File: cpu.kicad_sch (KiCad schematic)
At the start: 19 parts, among them J1 USB_C_Receptacle, SW1 TL3342F160QG/TR, U4 RP2040, U5 LM4040DBZ-3, U6 W25Q32JVSS, Y1 Crystal

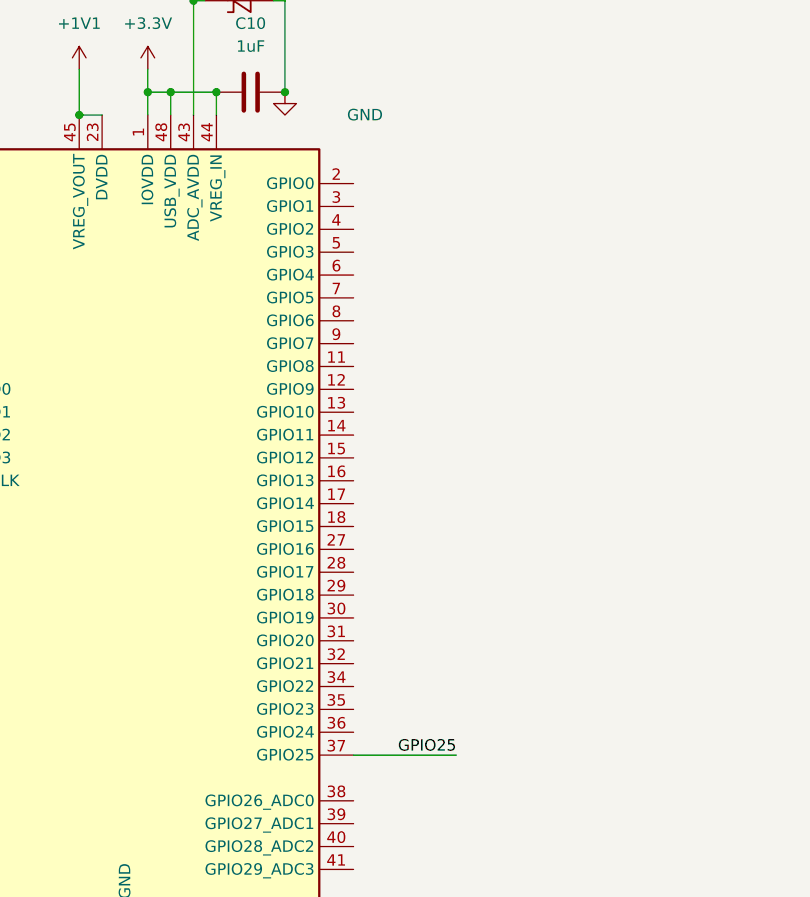
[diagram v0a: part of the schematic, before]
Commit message: Expanded IO
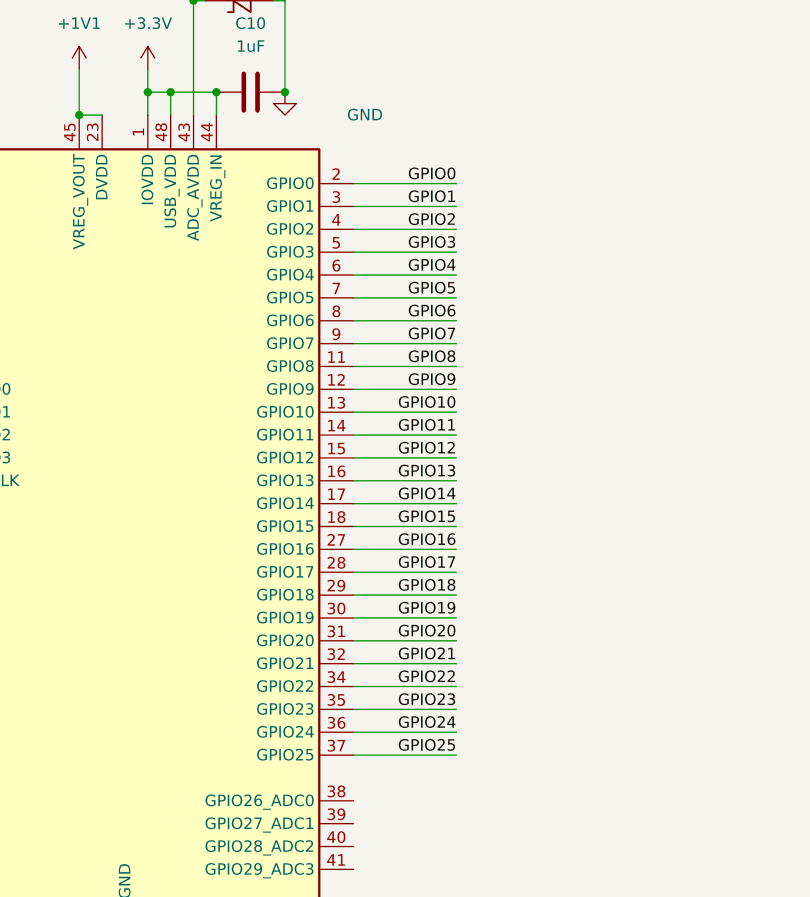
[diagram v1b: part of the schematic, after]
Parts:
- SW1: footprint SW_TL3342F160QG/TR -> TL3342F160QG_TR:SW_TL3342F160QG%2fTR
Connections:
- net GPIO8: now reaches U4.11 (GPIO8)
- net GPIO9: now reaches U4.12 (GPIO9)
- net GPIO10: now reaches U4.13 (GPIO10)
- net GPIO11: now reaches U4.14 (GPIO11)
- net GPIO12: now reaches U4.15 (GPIO12)
- net GPIO13: now reaches U4.16 (GPIO13)
- net GPIO14: now reaches U4.17 (GPIO14)
- net GPIO15: now reaches U4.18 (GPIO15)
- net GPIO0: now reaches U4.2 (GPIO0)
- net GPIO16: now reaches U4.27 (GPIO16)
- net GPIO17: now reaches U4.28 (GPIO17)
- net GPIO18: now reaches U4.29 (GPIO18)
- net GPIO1: now reaches U4.3 (GPIO1)
- net GPIO19: now reaches U4.30 (GPIO19)
- net GPIO20: now reaches U4.31 (GPIO20)
- net GPIO21: now reaches U4.32 (GPIO21)
- net GPIO22: now reaches U4.34 (GPIO22)
- net GPIO23: now reaches U4.35 (GPIO23)
- net GPIO24: now reaches U4.36 (GPIO24)
- net GPIO2: now reaches U4.4 (GPIO2)
- net GPIO3: now reaches U4.5 (GPIO3)
- net GPIO4: now reaches U4.6 (GPIO4)
- net GPIO5: now reaches U4.7 (GPIO5)
- net GPIO6: now reaches U4.8 (GPIO6)
- net GPIO7: now reaches U4.9 (GPIO7)

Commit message: Rev 1.0
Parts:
- added C17, C18, C19, C20, C21, C22, C23, C24: 0.1uF, Capacitor_SMD:C_0201_0603Metric, symbol Device:C
- added R15: 10k, Resistor_SMD:R_0603_1608Metric, symbol Device:R
- added SW2: TL3342F160QG/TR, TL3342F160QG_TR:SW_TL3342F160QG%2fTR, symbol TL3342F160QG_TR:TL3342F160QG/TR
- C10, C14: footprint (none) -> Capacitor_SMD:C_0201_0603Metric
- C11, C13: value 2u2F -> 27pF; footprint (none) -> Capacitor_SMD:C_0201_0603Metric
- C12: value 2u2F -> 0.1uF; footprint (none) -> Capacitor_SMD:C_0201_0603Metric
- D5: footprint (none) -> LED_SMD:LED_0201_0603Metric
- J1: footprint (none) -> Connector_USB:USB_C_Receptacle_HRO_TYPE-C-31-M-12
- R3, R4, R5, R6, R7, R8, R9: footprint (none) -> Resistor_SMD:R_0603_1608Metric
- Y1: footprint (none) -> Crystal:Crystal_SMD_3225-4Pin_3.2x2.5mm
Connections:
- net +1V1: now also C23.1, C24.1
- net +3.3V: now also C17.1, C18.1, C19.1, C20.1, C21.1, C22.1, R15.1
- net GND: now also C17.2, C18.2, C19.2, C20.2, C21.2, C22.2, C23.2, C24.2, SW2.1, SW2.2
- net RUN: now reaches U4.26 (RUN)
- net RUN: now also R15.2, SW2.3, SW2.4
- net GPIO26: now reaches U4.38 (GPIO26_ADC0)
- net GPIO27: now reaches U4.39 (GPIO27_ADC1)
- net GPIO28: now reaches U4.40 (GPIO28_ADC2)
- net GPIO29: now reaches U4.41 (GPIO29_ADC3)
- no-connect marks 0 -> 2
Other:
- note added: "Close to ADC_AVDD"
- note added: "Close to DVDD"
- note added: "Close to all IOVDD"
- title: (none) -> Iron Warriors v2.0 
- moved on the sheet: C10, C11, C13, C14, D5, R3, R4, R5, R8, R9, SW1, U4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

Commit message: Initial PCB view
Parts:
- C10, C11, C12, C13, C14, C17, C18, C19, C20, C21, C22, C23, C24: footprint Capacitor_SMD:C_0201_0603Metric -> Capacitor_SMD:C_0603_1608Metric
- D5: footprint LED_SMD:LED_0201_0603Metric -> LED_SMD:LED_0603_1608Metric
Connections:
- net XIN: now also Y1.2; no longer Y1.1
- net XOUT: now also Y1.1; no longer Y1.2
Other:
- moved on the sheet: Y1
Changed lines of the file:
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@@
   (title_block
     (title "Iron Warriors v2.0 ")
-    (date "2022-12-08")
+    (date "2022-12-13")
     (rev "1.0")
   )
@@
     (effects (font (size 1.27 1.27)) (justify left bottom))
   )
+  (hierarchical_label "GPIO23" (shape output) (at 141.605 114.3 0)
+    (effects (font (size 1.27 1.27)) (justify left))
+  )
+  (hierarchical_label "GPIO20" (shape output) (at 141.605 106.68 0)
+    (effects (font (size 1.27 1.27)) (justify left))
+  )
+  (hierarchical_label "GPIO21" (shape input) (at 141.605 109.22 0)
+    (effects (font (size 1.27 1.27)) (justify left))
+  )
+  (hierarchical_label "GPIO22" (shape input) (at 141.605 111.76 0)
+    (effects (font (size 1.27 1.27)) (justify left))
+  )
+  (hierarchical_label "GPIO25" (shape input) (at 141.605 119.38 0)
+    (effects (font (size 1.27 1.27)) (justify left))
+  )
+  (hierarchical_label "GPIO24" (shape input) (at 141.605 116.84 0)
+    (effects (font (size 1.27 1.27)) (justify left))
+  )
   (symbol (lib_id "Device:R") (at 218.44 25.4 0) (unit 1)
     (in_bom yes) (on_board yes)
@@
     (property "Reference" "C10" (id 0) (at 118.745 38.1 90))
     (property "Value" "1uF" (id 1) (at 118.745 40.64 90))
-    (property "Footprint" "Capacitor_SMD:C_0201_0603Metric" (id 2) (at 114.935 46.6852 0)
+    (property "Footprint" "Capacitor_SMD:C_0603_1608Metric" (id 2) (at 114.935 46.6852 0)
       (effects (font (size 1.27 1.27)) hide)
     )
@@
       (effects (font (size 1.27 1.27)) (justify left))
     )
-    (property "Footprint" "Capacitor_SMD:C_0201_0603Metric" (id 2) (at 84.7852 170.18 0)
+    (property "Footprint" "Capacitor_SMD:C_0603_1608Metric" (id 2) (at 84.7852 170.18 0)
       (effects (font (size 1.27 1.27)) hide)
     )
@@
     (property "Reference" "D5" (id 0) (at 242.2525 59.055 0))
     (property "Value" "LED" (id 1) (at 242.2525 61.595 0))
-    (property "Footprint" "LED_SMD:LED_0201_0603Metric" (id 2) (at 240.665 66.675 0)
+    (property "Footprint" "LED_SMD:LED_0603_1608Metric" (id 2) (at 240.665 66.675 0)
       (effects (font (size 1.27 1.27)) hide)
     )
@@
       (effects (font (size 1.27 1.27)) (justify left))
     )
-    (property "Footprint" "Capacitor_SMD:C_0201_0603Metric" (id 2) (at 115.2652 170.18 0)
+    (property "Footprint" "Capacitor_SMD:C_0603_1608Metric" (id 2) (at 115.2652 170.18 0)
       (effects (font (size 1.27 1.27)) hide)
     )
@@
       (effects (font (size 1.27 1.27)) (justify left))
     )
-    (property "Footprint" "Capacitor_SMD:C_0201_0603Metric" (id 2) (at 46.6852 170.18 0)
+    (property "Footprint" "Capacitor_SMD:C_0603_1608Metric" (id 2) (at 46.6852 170.18 0)
       (effects (font (size 1.27 1.27)) hide)
     )
@@
       (effects (font (size 1.27 1.27)) (justify left))
     )
-    (property "Footprint" "Capacitor_SMD:C_0201_0603Metric" (id 2) (at 247.9802 106.045 0)
+    (property "Footprint" "Capacitor_SMD:C_0603_1608Metric" (id 2) (at 247.9802 106.045 0)
       (effects (font (size 1.27 1.27)) hide)
     )
@@
     (pin "1")
   )
-  (symbol (lib_id "Device:Crystal") (at 238.125 98.425 0) (unit 1)
-    (in_bom yes) (on_board yes) (fields_autoplaced)
-    (property "Reference" "Y1" (id 0) (at 238.125 90.805 0))
-    (property "Value" "Crystal" (id 1) (at 238.125 93.345 0))
+  (symbol (lib_id "Device:Crystal") (at 238.125 98.425 180) (unit 1)
+    (in_bom yes) (on_board yes) (fields_autoplaced)
+    (property "Reference" "Y1" (id 0) (at 238.125 90.17 0))
+    (property "Value" "Crystal" (id 1) (at 238.125 92.71 0))
     (property "Footprint" "Crystal:Crystal_SMD_3225-4Pin_3.2x2.5mm" (id 2) (at 238.125 98.425 0)
       (effects (font (size 1.27 1.27)) hide)
@@
       (effects (font (size 1.27 1.27)) (justify left))
     )
-    (property "Footprint" "Capacitor_SMD:C_0201_0603Metric" (id 2) (at 97.4852 170.18 0)
+    (property "Footprint" "Capacitor_SMD:C_0603_1608Metric" (id 2) (at 97.4852 170.18 0)
       (effects (font (size 1.27 1.27)) hide)
     )
@@
       (effects (font (size 1.27 1.27)) (justify left))
     )
-    (property "Footprint" "Capacitor_SMD:C_0201_0603Metric" (id 2) (at 59.3852 170.18 0)
+    (property "Footprint" "Capacitor_SMD:C_0603_1608Metric" (id 2) (at 59.3852 170.18 0)
       (effects (font (size 1.27 1.27)) hide)
     )
@@
       (effects (font (size 1.27 1.27)) (justify left))
     )
-    (property "Footprint" "Capacitor_SMD:C_0201_0603Metric" (id 2) (at 253.0602 26.67 0)
+    (property "Footprint" "Capacitor_SMD:C_0603_1608Metric" (id 2) (at 253.0602 26.67 0)
       (effects (font (size 1.27 1.27)) hide)
     )
@@
       (effects (font (size 1.27 1.27)) (justify left))
     )
-    (property "Footprint" "Capacitor_SMD:C_0201_0603Metric" (id 2) (at 228.9302 106.045 0)
+    (property "Footprint" "Capacitor_SMD:C_0603_1608Metric" (id 2) (at 228.9302 106.045 0)
       (effects (font (size 1.27 1.27)) hide)
     )
@@
       (effects (font (size 1.27 1.27)) (justify left))
     )
-    (property "Footprint" "Capacitor_SMD:C_0201_0603Metric" (id 2) (at 33.9852 170.18 0)
+    (property "Footprint" "Capacitor_SMD:C_0603_1608Metric" (id 2) (at 33.9852 170.18 0)
       (effects (font (size 1.27 1.27)) hide)
     )
@@
       (effects (font (size 1.27 1.27)) (justify left))
     )
-    (property "Footprint" "Capacitor_SMD:C_0201_0603Metric" (id 2) (at 72.0852 170.18 0)
+    (property "Footprint" "Capacitor_SMD:C_0603_1608Metric" (id 2) (at 72.0852 170.18 0)
       (effects (font (size 1.27 1.27)) hide)
     )
@@
       (effects (font (size 1.27 1.27)) (justify left))
     )
-    (property "Footprint" "Capacitor_SMD:C_0201_0603Metric" (id 2) (at 141.9352 170.18 0)
+    (property "Footprint" "Capacitor_SMD:C_0603_1608Metric" (id 2) (at 141.9352 170.18 0)
       (effects (font (size 1.27 1.27)) hide)
     )
@@
       (effects (font (size 1.27 1.27)) (justify left))
     )
-    (property "Footprint" "Capacitor_SMD:C_0201_0603Metric" (id 2) (at 154.6352 170.18 0)
-      (effects (font (size 1.27 1.27)) hide)
-    )
+    (property "Footprint" "Capacitor_SMD:C_0603_1608Metric" (id 2) (at 154.6352 170.18 0)
+      (effects (font (size 1.27 1.27)) hide)
+    )

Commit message: First full version of the PCB
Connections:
- net GPIO11: now also R8.2
- net GPIO25: no longer R8.2
- net D+: now reaches R3.2, U4.47 (USB_DP)
- net D-: now reaches R4.2, U4.46 (USB_DM)
- no-connect marks 2 -> 14
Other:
- moved on the sheet: R3, R4
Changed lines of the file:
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@@
   (junction (at 45.72 162.56) (diameter 0) (color 0 0 0 0)
   )
+  (junction (at 109.855 45.72) (diameter 0) (color 0 0 0 0)
+  )
+  (junction (at 46.99 39.37) (diameter 0) (color 0 0 0 0)
+  )
+  (junction (at 162.56 21.59) (diameter 0) (color 0 0 0 0)
+  )
+  (junction (at 114.935 45.72) (diameter 0) (color 0 0 0 0)
+  )
+  (junction (at 170.18 44.45) (diameter 0) (color 0 0 0 0)
+  )
+  (junction (at 122.555 45.72) (diameter 0) (color 0 0 0 0)
+  )
+  (junction (at 31.75 87.63) (diameter 0) (color 0 0 0 0)
+  )
+  (junction (at 107.315 45.72) (diameter 0) (color 0 0 0 0)
+  )
+  (junction (at 162.56 53.975) (diameter 0) (color 0 0 0 0)
+  )
+  (junction (at 58.42 162.56) (diameter 0) (color 0 0 0 0)
+  )
   (junction (at 46.99 36.83) (diameter 0) (color 0 0 0 0)
   )
-  (junction (at 31.75 87.63) (diameter 0) (color 0 0 0 0)
-  )
-  (junction (at 109.855 45.72) (diameter 0) (color 0 0 0 0)
-  )
-  (junction (at 162.56 21.59) (diameter 0) (color 0 0 0 0)
-  )
-  (junction (at 114.935 45.72) (diameter 0) (color 0 0 0 0)
-  )
-  (junction (at 170.18 44.45) (diameter 0) (color 0 0 0 0)
-  )
-  (junction (at 46.99 39.37) (diameter 0) (color 0 0 0 0)
-  )
-  (junction (at 122.555 45.72) (diameter 0) (color 0 0 0 0)
-  )
-  (junction (at 107.315 45.72) (diameter 0) (color 0 0 0 0)
-  )
-  (junction (at 162.56 53.975) (diameter 0) (color 0 0 0 0)
-  )
-  (junction (at 58.42 162.56) (diameter 0) (color 0 0 0 0)
-  )
   (junction (at 79.375 55.88) (diameter 0) (color 0 0 0 0)
   )
@@
   (junction (at 140.97 162.56) (diameter 0) (color 0 0 0 0)
   )
+  (no_connect (at 46.99 46.99))
+  (no_connect (at 46.99 72.39))
+  (no_connect (at 46.99 62.23))
+  (no_connect (at 46.99 29.21))
+  (no_connect (at 46.99 64.77))
+  (no_connect (at 46.99 69.85))
+  (no_connect (at 46.99 77.47))
   (no_connect (at 79.375 121.92))
+  (no_connect (at 46.99 80.01))
+  (no_connect (at 46.99 57.15))
   (no_connect (at 79.375 124.46))
+  (no_connect (at 46.99 54.61))
+  (no_connect (at 46.99 49.53))
+  (no_connect (at 46.99 26.67))
   (wire (pts (xy 109.855 45.72) (xy 107.315 45.72))
     (stroke (width 0) (type default) (color 0 0 0 0))
   )
-  (wire (pts (xy 62.865 63.5) (xy 71.755 63.5))
+  (wire (pts (xy 52.07 63.5) (xy 60.96 63.5))
     (stroke (width 0) (type default) (color 0 0 0 0))
   )
@@
     (stroke (width 0) (type default) (color 0 0 0 0))
   )
+  (wire (pts (xy 68.58 66.04) (xy 79.375 66.04))
+    (stroke (width 0) (type default) (color 0 0 0 0))
+  )
   (wire (pts (xy 79.375 139.7) (xy 104.775 139.7))
     (stroke (width 0) (type default) (color 0 0 0 0))
@@
     (stroke (width 0) (type default) (color 0 0 0 0))
   )
+  (wire (pts (xy 68.58 63.5) (xy 79.375 63.5))
+    (stroke (width 0) (type default) (color 0 0 0 0))
+  )
   (wire (pts (xy 141.605 58.42) (xy 130.175 58.42))
     (stroke (width 0) (type default) (color 0 0 0 0))
   )
-  (wire (pts (xy 62.865 66.04) (xy 71.755 66.04))
+  (wire (pts (xy 52.07 66.04) (xy 60.96 66.04))
     (stroke (width 0) (type default) (color 0 0 0 0))
   )
@@
     (effects (font (size 1.27 1.27)) (justify right bottom))
   )
+  (label "D+" (at 71.755 63.5 0)
+    (effects (font (size 1.27 1.27)) (justify left bottom))
+  )
+  (label "D-" (at 71.755 66.04 0)
+    (effects (font (size 1.27 1.27)) (justify left bottom))
+  )
   (label "QSPI_SD3" (at 264.16 45.72 180)
     (effects (font (size 1.27 1.27)) (justify right bottom))
@@
     (effects (font (size 1.27 1.27)) (justify right bottom))
   )
-  (label "USB_DP" (at 62.865 63.5 0)
+  (label "USB_DP" (at 52.07 63.5 0)
     (effects (font (size 1.27 1.27)) (justify left bottom))
   )
@@
     (effects (font (size 1.27 1.27)) (justify right bottom))
   )
-  (label "USB_DM" (at 62.865 66.04 0)
+  (label "USB_DM" (at 52.07 66.04 0)
     (effects (font (size 1.27 1.27)) (justify left bottom))
   )
@@
     (effects (font (size 1.27 1.27)) (justify right bottom))
   )
-  (label "GPIO25" (at 217.805 66.675 0)
+  (label "GPIO11" (at 217.805 66.675 0)
     (effects (font (size 1.27 1.27)) (justify left bottom))
   )
@@
     (pin "2")
   )
-  (symbol (lib_id "Device:R") (at 75.565 63.5 90) (unit 1)
+  (symbol (lib_id "Device:R") (at 64.77 63.5 90) (unit 1)
     (in_bom yes) (on_board yes)
-    (property "Reference" "R3" (id 0) (at 75.565 60.96 90))
-    (property "Value" "27" (id 1) (at 75.565 63.5 90))
-    (property "Footprint" "Resistor_SMD:R_0603_1608Metric" (id 2) (at 75.565 65.278 90)
-      (effects (font (size 1.27 1.27)) hide)
-    )
-    (property "Datasheet" "~" (id 3) (at 75.565 63.5 0)
+    (property "Reference" "R3" (id 0) (at 64.77 60.96 90))
+    (property "Value" "27" (id 1) (at 64.77 63.5 90))
+    (property "Footprint" "Resistor_SMD:R_0603_1608Metric" (id 2) (at 64.77 65.278 90)
+      (effects (font (size 1.27 1.27)) hide)
+    )
+    (property "Datasheet" "~" (id 3) (at 64.77 63.5 0)
       (effects (font (size 1.27 1.27)) hide)
     )
@@
     )
     (pin "1")
+  )
+  (symbol (lib_id "Device:C") (at 114.3 166.37 0) (unit 1)
+    (in_bom yes) (on_board yes) (fields_autoplaced)
+    (property "Reference" "C22" (id 0) (at 118.11 165.0999 0)
+      (effects (font (size 1.27 1.27)) (justify left))
+    )
+    (property "Value" "0.1uF" (id 1) (at 118.11 167.6399 0)
+      (effects (font (size 1.27 1.27)) (justify left))
+    )
+    (property "Footprint" "Capacitor_SMD:C_0603_1608Metric" (id 2) (at 115.2652 170.18 0)
+      (effects (font (size 1.27 1.27)) hide)
+    )
+    (property "Datasheet" "~" (id 3) (at 114.3 166.37 0)
+      (effects (font (size 1.27 1.27)) hide)
+    )
+    (pin "1")
+    (pin "2")
   )
   (symbol (lib_id "Connector:USB_C_Receptacle") (at 31.75 46.99 0) (unit 1)
@@
     (pin "S1")
   )
-  (symbol (lib_id "Device:C") (at 114.3 166.37 0) (unit 1)
-    (in_bom yes) (on_board yes) (fields_autoplaced)
-    (property "Reference" "C22" (id 0) (at 118.11 165.0999 0)
-      (effects (font (size 1.27 1.27)) (justify left))
-    )
-    (property "Value" "0.1uF" (id 1) (at 118.11 167.6399 0)
-      (effects (font (size 1.27 1.27)) (justify left))
-    )
-    (property "Footprint" "Capacitor_SMD:C_0603_1608Metric" (id 2) (at 115.2652 170.18 0)
-      (effects (font (size 1.27 1.27)) hide)
-    )
-    (property "Datasheet" "~" (id 3) (at 114.3 166.37 0)
-      (effects (font (size 1.27 1.27)) hide)
-    )
-    (pin "1")
-    (pin "2")
-  )
   (symbol (lib_id "power:+3.3V") (at 79.375 40.005 0) (unit 1)
     (in_bom yes) (on_board yes) (fields_autoplaced)
@@
     (pin "2")
   )
-  (symbol (lib_id "Device:R") (at 75.565 66.04 90) (unit 1)
+  (symbol (lib_id "Device:R") (at 64.77 66.04 90) (unit 1)
     (in_bom yes) (on_board yes)
-    (property "Reference" "R4" (id 0) (at 75.565 68.58 90))
-    (property "Value" "27" (id 1) (at 75.565 66.04 90))
-    (property "Footprint" "Resistor_SMD:R_0603_1608Metric" (id 2) (at 75.565 67.818 90)
-      (effects (font (size 1.27 1.27)) hide)
-    )
-    (property "Datasheet" "~" (id 3) (at 75.565 66.04 0)
-      (effects (font (size 1.27 1.27)) hide)
-    )
+    (property "Reference" "R4" (id 0) (at 64.77 68.58 90))
+    (property "Value" "27" (id 1) (at 64.77 66.04 90))
+    (property "Footprint" "Resistor_SMD:R_0603_1608Metric" (id 2) (at 64.77 67.818 90)
+      (effects (font (size 1.27 1.27)) hide)
+    )
+    (property "Datasheet" "~" (id 3) (at 64.77 66.04 0)
+      (effects (font (size 1.27 1.27)) hide)
+    )
